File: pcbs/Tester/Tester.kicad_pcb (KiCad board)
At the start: 2 copper layers, 17 parts, among them J201 Raspberry_Pi_2_3, U201 SN74LVC4245APWR, U202 SN74LVC4245APWR, U301 74HC595, U302 74HC595, U303 74HC595, U401 74HC165, U402 74HC165, U403 74HC165

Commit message: Lots of rethinking
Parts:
- added J301: Conn_02x20_Odd_Even, Connector_PinHeader_2.54mm:PinHeader_2x20_P2.54mm_Vertical, F.Cu at (147.3, 33.0)
- added J401: Conn_02x20_Odd_Even, Connector_PinHeader_2.54mm:PinHeader_2x20_P2.54mm_Vertical, F.Cu at (147.3, 104.1)
- added R301: 1M, Resistor_SMD:R_0603_1608Metric, F.Cu at (139.7, 33.0)
- added R302: 1M, Resistor_SMD:R_0603_1608Metric, F.Cu at (157.5, 33.0)
- added R303: 1M, Resistor_SMD:R_0603_1608Metric, F.Cu at (139.7, 35.6)
- added R304: 1M, Resistor_SMD:R_0603_1608Metric, F.Cu at (157.5, 35.6)
- added R305: 1M, Resistor_SMD:R_0603_1608Metric, F.Cu at (139.7, 38.1)
- added R306: 1M, Resistor_SMD:R_0603_1608Metric, F.Cu at (157.5, 38.1)
- added R307: 1M, Resistor_SMD:R_0603_1608Metric, F.Cu at (139.7, 40.6)
- added R308: 1M, Resistor_SMD:R_0603_1608Metric, F.Cu at (157.5, 40.6)
- added R309: 1M, Resistor_SMD:R_0603_1608Metric, F.Cu at (139.7, 43.2)
- added R310: 1M, Resistor_SMD:R_0603_1608Metric, F.Cu at (157.5, 43.2)
- added R311: 1M, Resistor_SMD:R_0603_1608Metric, F.Cu at (139.7, 45.7)
- added R312: 1M, Resistor_SMD:R_0603_1608Metric, F.Cu at (157.5, 45.7)
- added R313: 1M, Resistor_SMD:R_0603_1608Metric, F.Cu at (139.7, 48.3)
- added R314: 1M, Resistor_SMD:R_0603_1608Metric, F.Cu at (157.5, 48.3)
- added R315: 1M, Resistor_SMD:R_0603_1608Metric, F.Cu at (139.7, 50.8)
- added R316: 1M, Resistor_SMD:R_0603_1608Metric, F.Cu at (157.5, 50.8)
- added R317: 1M, Resistor_SMD:R_0603_1608Metric, F.Cu at (139.7, 53.3)
- added R318: 1M, Resistor_SMD:R_0603_1608Metric, F.Cu at (157.5, 53.3)
- added R319: 1M, Resistor_SMD:R_0603_1608Metric, F.Cu at (139.8, 55.9)
- added R320: 1M, Resistor_SMD:R_0603_1608Metric, F.Cu at (157.5, 55.9)
- added R321: 1M, Resistor_SMD:R_0603_1608Metric, F.Cu at (139.8, 58.4)
- added R322: 1M, Resistor_SMD:R_0603_1608Metric, F.Cu at (157.5, 58.4)
- added R323: 1M, Resistor_SMD:R_0603_1608Metric, F.Cu at (139.7, 61.0)
- added R324: 1M, Resistor_SMD:R_0603_1608Metric, F.Cu at (157.5, 61.0)
- added R325: 1M, Resistor_SMD:R_0603_1608Metric, F.Cu at (139.7, 63.5)
- added R326: 1M, Resistor_SMD:R_0603_1608Metric, F.Cu at (157.5, 63.5)
- added R327: 1M, Resistor_SMD:R_0603_1608Metric, F.Cu at (139.7, 66.0)
- added R328: 1M, Resistor_SMD:R_0603_1608Metric, F.Cu at (157.5, 66.0)
- added R329: 1M, Resistor_SMD:R_0603_1608Metric, F.Cu at (139.7, 68.6)
- added R330: 1M, Resistor_SMD:R_0603_1608Metric, F.Cu at (157.5, 68.6)
- added R331: 1M, Resistor_SMD:R_0603_1608Metric, F.Cu at (139.7, 71.1)
- added R332: 1M, Resistor_SMD:R_0603_1608Metric, F.Cu at (157.5, 71.1)
- added R333: 1M, Resistor_SMD:R_0603_1608Metric, F.Cu at (139.7, 73.7)
- added R334: 1M, Resistor_SMD:R_0603_1608Metric, F.Cu at (157.5, 73.7)
- added R335: 1M, Resistor_SMD:R_0603_1608Metric, F.Cu at (139.7, 76.2)
- added R336: 1M, Resistor_SMD:R_0603_1608Metric, F.Cu at (157.5, 76.2)
- added R337: 1M, Resistor_SMD:R_0603_1608Metric, F.Cu at (139.7, 78.7)
- added R338: 1M, Resistor_SMD:R_0603_1608Metric, F.Cu at (157.5, 78.7)
- added R339: 1M, Resistor_SMD:R_0603_1608Metric, F.Cu at (139.7, 81.3)
- added R340: 1M, Resistor_SMD:R_0603_1608Metric, F.Cu at (157.5, 81.3)
- added R409: 1M, Resistor_SMD:R_0603_1608Metric, F.Cu at (139.7, 114.3)
- added R410: 1M, Resistor_SMD:R_0603_1608Metric, F.Cu at (157.5, 114.3)
- added R411: 1M, Resistor_SMD:R_0603_1608Metric, F.Cu at (139.7, 116.8)
- added R412: 1M, Resistor_SMD:R_0603_1608Metric, F.Cu at (157.5, 116.8)
- added R413: 1M, Resistor_SMD:R_0603_1608Metric, F.Cu at (139.7, 119.4)
- added R414: 1M, Resistor_SMD:R_0603_1608Metric, F.Cu at (157.5, 119.4)
- added R415: 1M, Resistor_SMD:R_0603_1608Metric, F.Cu at (139.7, 121.9)
- added R416: 1M, Resistor_SMD:R_0603_1608Metric, F.Cu at (157.5, 121.9)
- added R417: 1M, Resistor_SMD:R_0603_1608Metric, F.Cu at (139.7, 124.5)
- added R418: 1M, Resistor_SMD:R_0603_1608Metric, F.Cu at (157.5, 124.5)
- added R419: 1M, Resistor_SMD:R_0603_1608Metric, F.Cu at (139.7, 127.0)
- added R420: 1M, Resistor_SMD:R_0603_1608Metric, F.Cu at (157.5, 127.0)
- added R421: 1M, Resistor_SMD:R_0603_1608Metric, F.Cu at (139.7, 129.5)
- added R422: 1M, Resistor_SMD:R_0603_1608Metric, F.Cu at (157.5, 129.5)
- added R423: 1M, Resistor_SMD:R_0603_1608Metric, F.Cu at (139.7, 132.1)
- added R424: 1M, Resistor_SMD:R_0603_1608Metric, F.Cu at (157.5, 132.1)
- added R425: 1M, Resistor_SMD:R_0603_1608Metric, F.Cu at (139.7, 134.6)
- added R426: 1M, Resistor_SMD:R_0603_1608Metric, F.Cu at (157.5, 134.6)
- added R427: 1M, Resistor_SMD:R_0603_1608Metric, F.Cu at (139.7, 137.2)
- added R428: 1M, Resistor_SMD:R_0603_1608Metric, F.Cu at (157.5, 137.2)
- added R429: 1M, Resistor_SMD:R_0603_1608Metric, F.Cu at (139.7, 139.7)
- added R430: 1M, Resistor_SMD:R_0603_1608Metric, F.Cu at (157.5, 139.7)
- added R431: 1M, Resistor_SMD:R_0603_1608Metric, F.Cu at (139.7, 142.2)
- added R432: 1M, Resistor_SMD:R_0603_1608Metric, F.Cu at (157.5, 142.2)
- added R433: 1M, Resistor_SMD:R_0603_1608Metric, F.Cu at (139.7, 144.8)
- added R434: 1M, Resistor_SMD:R_0603_1608Metric, F.Cu at (157.5, 144.8)
- added R435: 1M, Resistor_SMD:R_0603_1608Metric, F.Cu at (139.7, 147.3)
- added R436: 1M, Resistor_SMD:R_0603_1608Metric, F.Cu at (157.5, 147.3)
- added R437: 1M, Resistor_SMD:R_0603_1608Metric, F.Cu at (139.7, 149.9)
- added R438: 1M, Resistor_SMD:R_0603_1608Metric, F.Cu at (157.5, 149.9)
- added R439: 1M, Resistor_SMD:R_0603_1608Metric, F.Cu at (139.7, 152.4)
- added R440: 1M, Resistor_SMD:R_0603_1608Metric, F.Cu at (157.5, 152.4)
- added U203: SN74LVC4245APWR, Package_SO:TSSOP-24_4.4x7.8mm_P0.65mm, F.Cu at (96.5, 132.1)
- added U304: 74HC595, Package_SO:SO-16_3.9x9.9mm_P1.27mm, F.Cu at (121.9, 68.6)
- added U305: 74HC595, Package_SO:SO-16_3.9x9.9mm_P1.27mm, F.Cu at (121.9, 78.7)
- added U403: 74HC165, Package_SO:SOIC-16_3.9x9.9mm_P1.27mm, F.Cu at (121.9, 127.0)
- added U404: 74HC165, Package_SO:SOIC-16_3.9x9.9mm_P1.27mm, F.Cu at (121.9, 137.2)
- moved U301 53.4 mm to (121.9, 38.1)
- moved U302 45.0 mm to (121.9, 48.3)
- moved U303 37.5 mm to (121.9, 58.4)
- moved U201 35.7 mm to (99.1, 58.4)
- moved U405 34.7 mm to (121.9, 147.3)
- moved R408 33.1 mm to (157.5, 111.8), turned to 0 degrees
- moved R406 30.6 mm to (157.5, 109.2), turned to 0 degrees
- moved R404 29.0 mm to (157.5, 106.7), turned to 0 degrees
- moved R402 28.4 mm to (157.5, 104.1), turned to 0 degrees
- moved R401 26.5 mm to (139.7, 104.1), turned to 180 degrees
- moved R403 23.0 mm to (139.7, 106.7), turned to 180 degrees
- moved R405 20.5 mm to (139.7, 109.2), turned to 180 degrees
- moved R407 19.3 mm to (139.7, 111.8), turned to 180 degrees
- moved J201 15.5 mm to (78.7, 68.6)
- moved U402 12.7 mm to (121.9, 116.8)
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- renumbered U403 to U405
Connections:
- R401 pad 1: /In Registers/IN0 -> /In Registers/In_{0}
- R402 pad 1: /In Registers/IN1 -> /In Registers/In_{1}
- R403 pad 1: /In Registers/IN2 -> /In Registers/In_{2}
- R404 pad 1: /In Registers/IN3 -> /In Registers/In_{3}
- R405 pad 1: /In Registers/IN4 -> /In Registers/In_{4}
- R406 pad 1: /In Registers/IN5 -> /In Registers/In_{5}
- R407 pad 1: /In Registers/IN6 -> /In Registers/In_{6}
- R408 pad 1: /In Registers/IN7 -> /In Registers/In_{7}
- U201 pad 10: unconnected-(U201-Pad10) -> /Out Registers/~{OE5}
- U201 pad 14: GND -> /Pi Input/~{SPI0_{OE1}}
- U201 pad 15: /Pi Input/SPI1_{CLK} -> /Pi Input/~{SPI0_{OE1}}
- U201 pad 16: /Pi Input/~{SPI1_{LOAD}} -> /Pi Input/~{SPI0_{OE1}}
- U201 pad 17: /Pi Input/~{SPI1_{SELECT}} -> /Pi Input/~{SPI0_{OE1}}
- U201 pad 18: GND -> /Pi Input/~{SPI0_{OE1}}
- U201 pad 6: unconnected-(U201-Pad6) -> /Out Registers/~{OE1}
- U201 pad 7: /Pi Input/~{IN_{SELECT}} -> /Out Registers/~{OE2}
- U201 pad 8: /Pi Input/~{IN_{LOAD}} -> /Out Registers/~{OE3}
- U201 pad 9: /Pi Input/IN_{CLK} -> /Out Registers/~{OE4}
- U301 pad 1: unconnected-(U301-Pad1) -> /Out Registers/Out_{1}
- U301 pad 13: GND -> /Out Registers/~{OE1}
- U301 pad 15: unconnected-(U301-Pad15) -> /Out Registers/Out_{0}
- U301 pad 2: unconnected-(U301-Pad2) -> /Out Registers/Out_{2}
- U301 pad 3: unconnected-(U301-Pad3) -> /Out Registers/Out_{3}
- U301 pad 4: unconnected-(U301-Pad4) -> /Out Registers/Out_{4}
- U301 pad 5: unconnected-(U301-Pad5) -> /Out Registers/Out_{5}
- U301 pad 6: unconnected-(U301-Pad6) -> /Out Registers/Out_{6}
- U301 pad 7: unconnected-(U301-Pad7) -> /Out Registers/Out_{7}
- U302 pad 1: unconnected-(U302-Pad1) -> /Out Registers/Out_{9}
- U302 pad 13: GND -> /Out Registers/~{OE2}
- U302 pad 15: unconnected-(U302-Pad15) -> /Out Registers/Out_{8}
- U302 pad 2: unconnected-(U302-Pad2) -> /Out Registers/Out_{10}
- U302 pad 3: unconnected-(U302-Pad3) -> /Out Registers/Out_{11}
- U302 pad 4: unconnected-(U302-Pad4) -> /Out Registers/Out_{12}
- U302 pad 5: unconnected-(U302-Pad5) -> /Out Registers/Out_{13}
- U302 pad 6: unconnected-(U302-Pad6) -> /Out Registers/Out_{14}
- U302 pad 7: unconnected-(U302-Pad7) -> /Out Registers/Out_{15}
- U303 pad 13: GND -> /Out Registers/~{OE3}
- U303 pad 9: unconnected-(U303-Pad9) -> Net-(U303-Pad9)
- U401 pad 10: GND -> Net-(U401-Pad10)
- U401 pad 11: /In Registers/IN23 -> /In Registers/In_{7}
- U401 pad 12: /In Registers/IN22 -> /In Registers/In_{6}
- U401 pad 13: /In Registers/IN21 -> /In Registers/In_{5}
- U401 pad 14: /In Registers/IN20 -> /In Registers/In_{4}
- U401 pad 3: /In Registers/IN19 -> /In Registers/In_{3}
- U401 pad 4: /In Registers/IN18 -> /In Registers/In_{2}
- U401 pad 5: /In Registers/IN17 -> /In Registers/In_{1}
- U401 pad 6: /In Registers/IN16 -> /In Registers/In_{0}
- U401 pad 9: Net-(U401-Pad9) -> /In Registers/IN_{DATA}
- U402 pad 10: Net-(U401-Pad9) -> Net-(U403-Pad9)
- U402 pad 9: Net-(U402-Pad9) -> Net-(U401-Pad10)
- U405 pad 10: Net-(U402-Pad9) -> GND
- U405 pad 11: /In Registers/IN7 -> unconnected-(U405-Pad11)
- U405 pad 12: /In Registers/IN6 -> unconnected-(U405-Pad12)
- U405 pad 13: /In Registers/IN5 -> unconnected-(U405-Pad13)
- U405 pad 14: /In Registers/IN4 -> unconnected-(U405-Pad14)
- U405 pad 3: /In Registers/IN3 -> unconnected-(U405-Pad3)
- U405 pad 4: /In Registers/IN2 -> unconnected-(U405-Pad4)
- U405 pad 5: /In Registers/IN1 -> unconnected-(U405-Pad5)
- U405 pad 6: /In Registers/IN0 -> unconnected-(U405-Pad6)
- U405 pad 9: /In Registers/IN_{DATA} -> Net-(U404-Pad10)

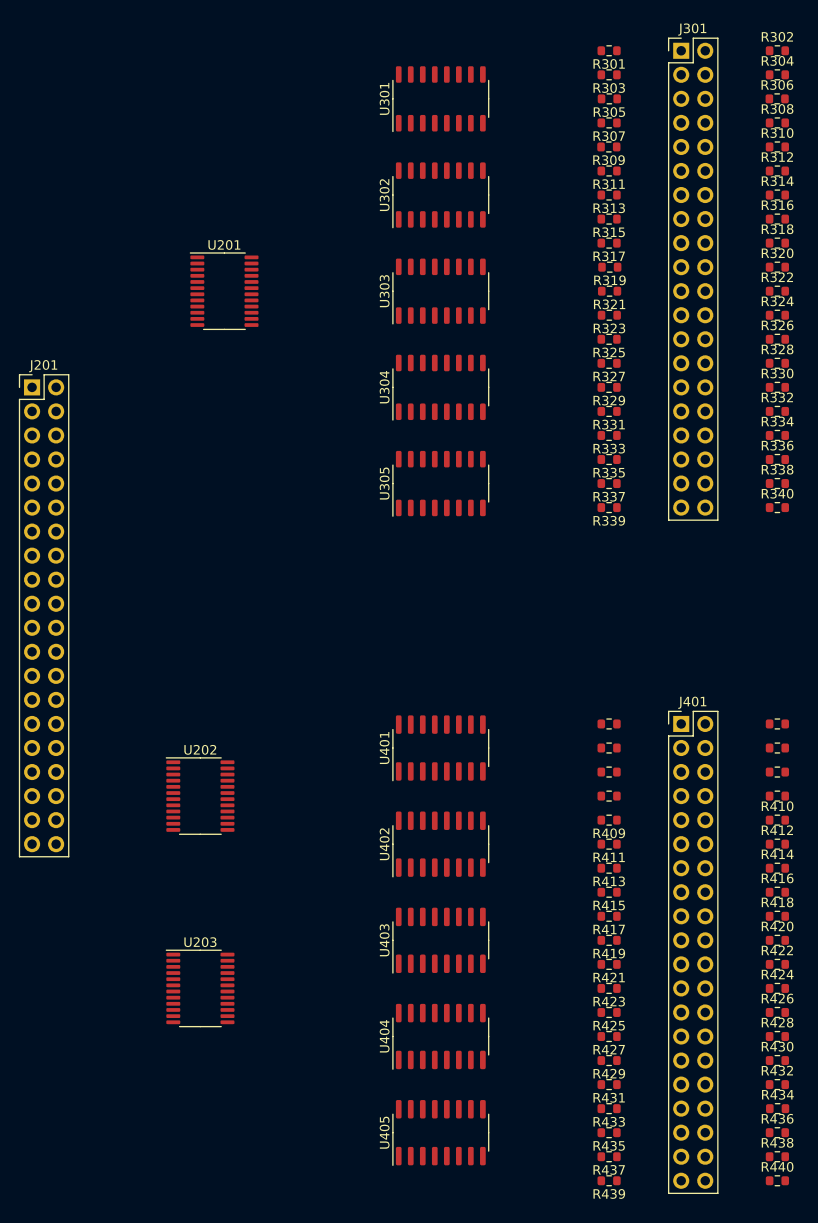
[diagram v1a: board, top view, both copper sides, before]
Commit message: Routing output side
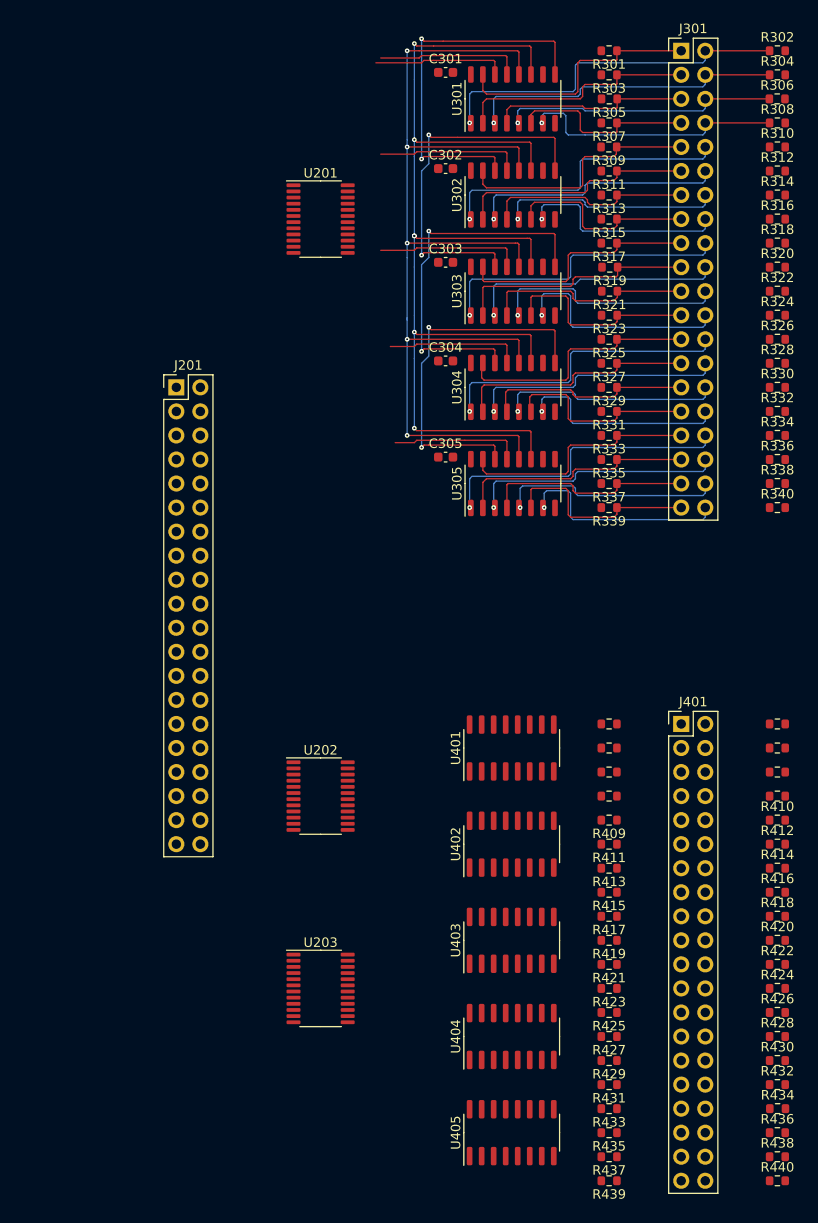
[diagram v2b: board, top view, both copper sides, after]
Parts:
- added C301: 100n, Capacitor_SMD:C_0603_1608Metric, F.Cu at (122.4, 35.3)
- added C302: 100n, Capacitor_SMD:C_0603_1608Metric, F.Cu at (122.4, 45.5)
- added C303: 100n, Capacitor_SMD:C_0603_1608Metric, F.Cu at (122.4, 55.4)
- added C304: 100n, Capacitor_SMD:C_0603_1608Metric, F.Cu at (122.4, 65.8)
- added C305: 100n, Capacitor_SMD:C_0603_1608Metric, F.Cu at (122.4, 75.9)
- moved J201 15.2 mm to (94.0, 68.6)
- moved U202 12.7 mm to (109.2, 111.8)
- moved U203 12.7 mm to (109.2, 132.1)
- moved U201 12.7 mm to (109.2, 50.8)
- moved U301 7.62 mm to (129.5, 38.1)
- moved U302 7.62 mm to (129.5, 48.3)
- moved U303 7.62 mm to (129.5, 58.4)
- moved U304 7.62 mm to (129.5, 68.6)
- moved U305 7.62 mm to (129.5, 78.7)
- moved U401 7.49 mm to (129.4, 106.7)
- moved U402 7.49 mm to (129.4, 116.8)
- moved U403 7.49 mm to (129.4, 127.0)
- moved U404 7.49 mm to (129.4, 137.2)
- moved U405 7.49 mm to (129.4, 147.3)
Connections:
- U303 pad 1: unconnected-(U303-Pad1) -> /Out Registers/Out_{17}
- U303 pad 15: unconnected-(U303-Pad15) -> /Out Registers/Out_{16}
- U303 pad 2: unconnected-(U303-Pad2) -> /Out Registers/Out_{18}
- U303 pad 3: unconnected-(U303-Pad3) -> /Out Registers/Out_{19}
- U303 pad 4: unconnected-(U303-Pad4) -> /Out Registers/Out_{20}
- U303 pad 5: unconnected-(U303-Pad5) -> /Out Registers/Out_{21}
- U303 pad 6: unconnected-(U303-Pad6) -> /Out Registers/Out_{22}
- U303 pad 7: unconnected-(U303-Pad7) -> /Out Registers/Out_{23}
- U304 pad 1: unconnected-(U304-Pad1) -> /Out Registers/Out_{25}
- U304 pad 15: unconnected-(U304-Pad15) -> /Out Registers/Out_{24}
- U304 pad 2: unconnected-(U304-Pad2) -> /Out Registers/Out_{26}
- U304 pad 3: unconnected-(U304-Pad3) -> /Out Registers/Out_{27}
- U304 pad 4: unconnected-(U304-Pad4) -> /Out Registers/Out_{28}
- U304 pad 5: unconnected-(U304-Pad5) -> /Out Registers/Out_{29}
- U304 pad 6: unconnected-(U304-Pad6) -> /Out Registers/Out_{30}
- U304 pad 7: unconnected-(U304-Pad7) -> /Out Registers/Out_{31}
- U305 pad 1: unconnected-(U305-Pad1) -> /Out Registers/Out_{33}
- U305 pad 15: unconnected-(U305-Pad15) -> /Out Registers/Out_{32}
- U305 pad 2: unconnected-(U305-Pad2) -> /Out Registers/Out_{34}
- U305 pad 3: unconnected-(U305-Pad3) -> /Out Registers/Out_{35}
- U305 pad 4: unconnected-(U305-Pad4) -> /Out Registers/Out_{36}
- U305 pad 5: unconnected-(U305-Pad5) -> /Out Registers/Out_{37}
- U305 pad 6: unconnected-(U305-Pad6) -> /Out Registers/Out_{38}
- U305 pad 7: unconnected-(U305-Pad7) -> /Out Registers/Out_{39}
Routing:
- net /Out Registers/OUT_{CLK}: track 0.00 -> 117.5 mm, vias 0 -> 6
- net /Out Registers/~{OUT_{SELECT}}: track 0.00 -> 112.1 mm, vias 0 -> 5
- net Net-(U301-Pad9): track 0.00 -> 39.6 mm, vias 0 -> 2
- net Net-(U304-Pad9): track 0.00 -> 39.2 mm, vias 0 -> 2
- net Net-(U302-Pad9): track 0.00 -> 39.2 mm, vias 0 -> 2
- net Net-(U303-Pad9): track 0.00 -> 39.2 mm, vias 0 -> 2
- net /Out Registers/Out_{1}: track 0.00 -> 38.7 mm, vias 0 -> 1
- net /Out Registers/Out_{3}: track 0.00 -> 33.6 mm, vias 0 -> 1
- net /Out Registers/Out_{25}: track 0.00 -> 31.9 mm, vias 0 -> 1
- net /Out Registers/Out_{33}: track 0.00 -> 31.9 mm, vias 0 -> 1
- net /Out Registers/Out_{17}: track 0.00 -> 31.9 mm, vias 0 -> 1
- net /Out Registers/Out_{9}: track 0.00 -> 31.9 mm, vias 0 -> 1
- net /Out Registers/Out_{5}: track 0.00 -> 29.2 mm, vias 0 -> 1
- net /Out Registers/Out_{7}: track 0.00 -> 28.0 mm, vias 0 -> 1
- net /Out Registers/Out_{0}: track 0.00 -> 27.0 mm
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
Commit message: Thinking about the input side
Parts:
- added C401: 100n, Capacitor_SMD:C_0603_1608Metric, F.Cu at (122.4, 106.4)
- added C402: 100n, Capacitor_SMD:C_0603_1608Metric, F.Cu at (122.4, 116.6)
- added C403: 100n, Capacitor_SMD:C_0603_1608Metric, F.Cu at (122.4, 126.7)
- added C404: 100n, Capacitor_SMD:C_0603_1608Metric, F.Cu at (122.4, 136.9)
- added C405: 100n, Capacitor_SMD:C_0603_1608Metric, F.Cu at (122.4, 147.1)
- moved U405 2.54 mm to (129.5, 149.9)
- moved U401 2.54 mm to (129.5, 109.2)
- moved U402 2.54 mm to (129.5, 119.4)
- moved U403 2.54 mm to (129.5, 129.5)
- moved U404 2.54 mm to (129.5, 139.7)
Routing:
- net /In Registers/In_{1}: track 0.00 -> 13.6 mm
- net /In Registers/In_{5}: track 0.00 -> 13.3 mm
- net /In Registers/In_{3}: track 0.00 -> 13.3 mm
- net /In Registers/In_{0}: track 0.00 -> 3.94 mm
- net /In Registers/In_{4}: track 0.00 -> 3.69 mm
- net /In Registers/In_{6}: track 0.00 -> 3.69 mm
- net /In Registers/In_{2}: track 0.00 -> 3.69 mm
